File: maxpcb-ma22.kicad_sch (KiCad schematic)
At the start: 28 parts, among them P1 USB_C_Plug_USB2.0, SW1 SW_Push, U1 ATmega32U4-A, Y1 16mHz

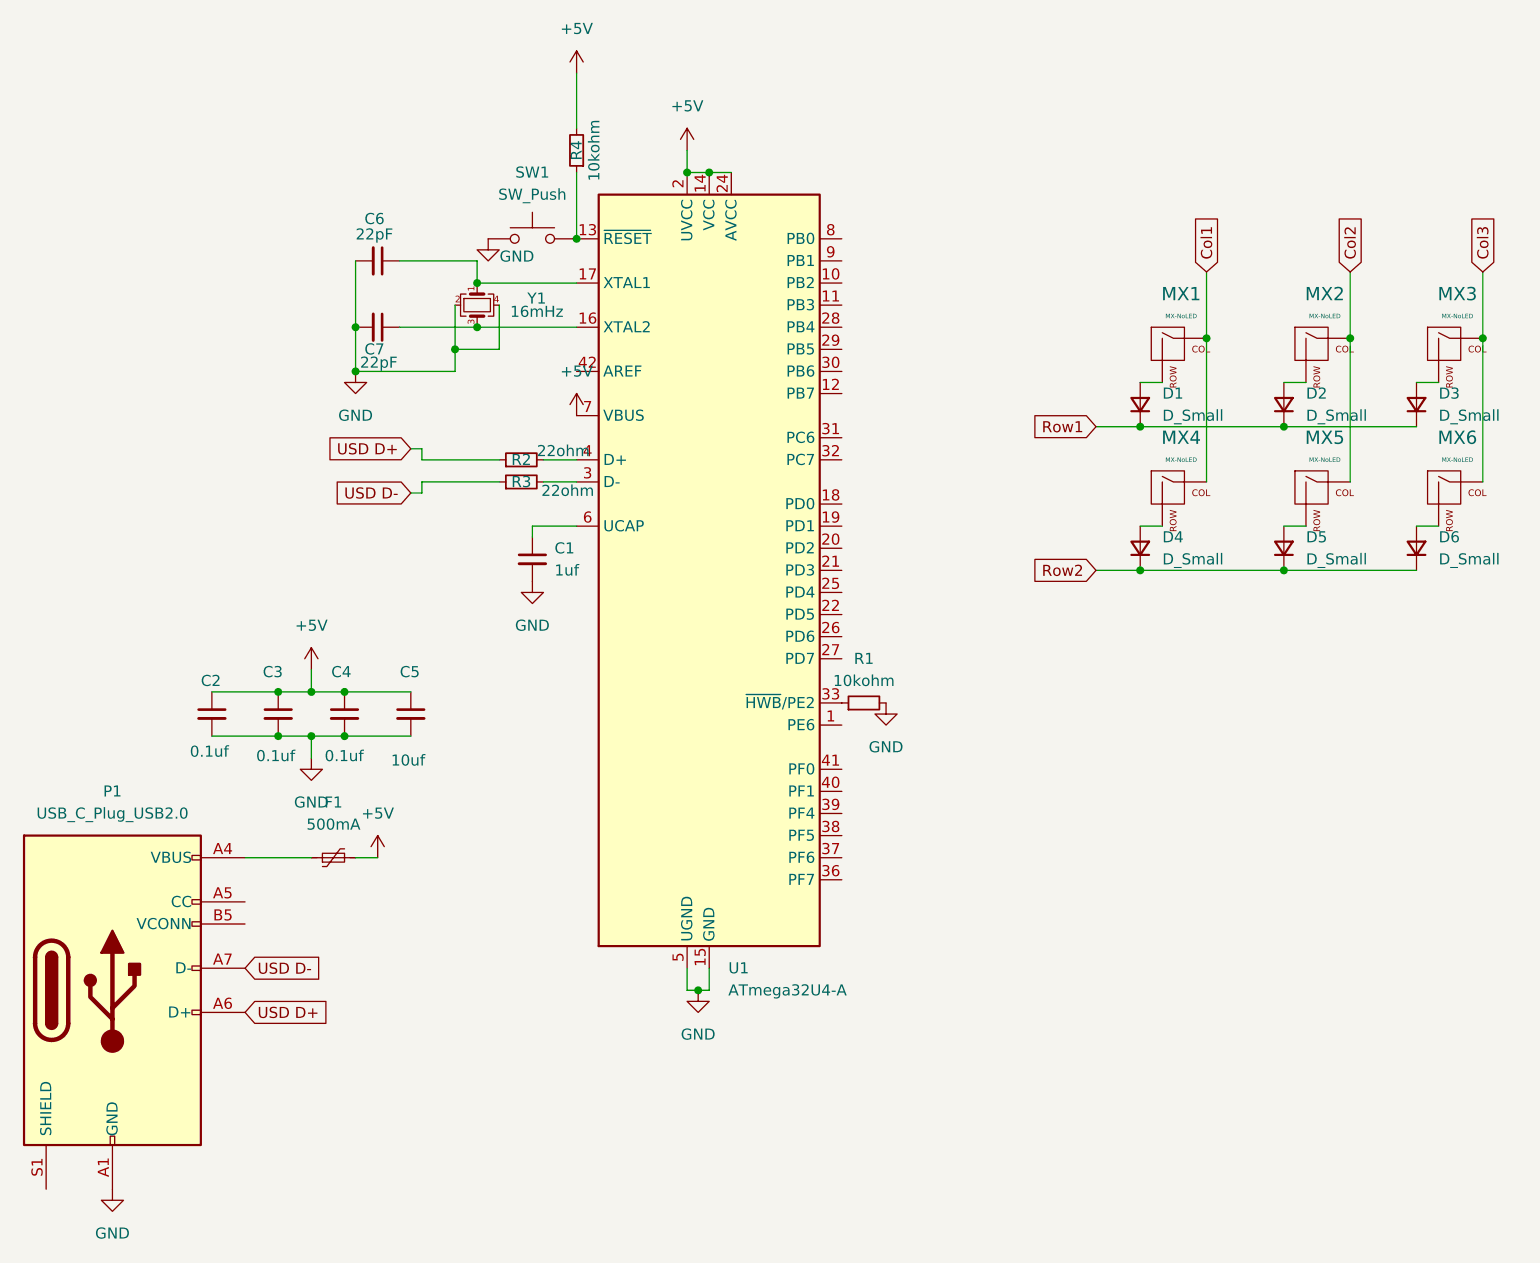
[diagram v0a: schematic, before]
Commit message: complete redo with 32u4
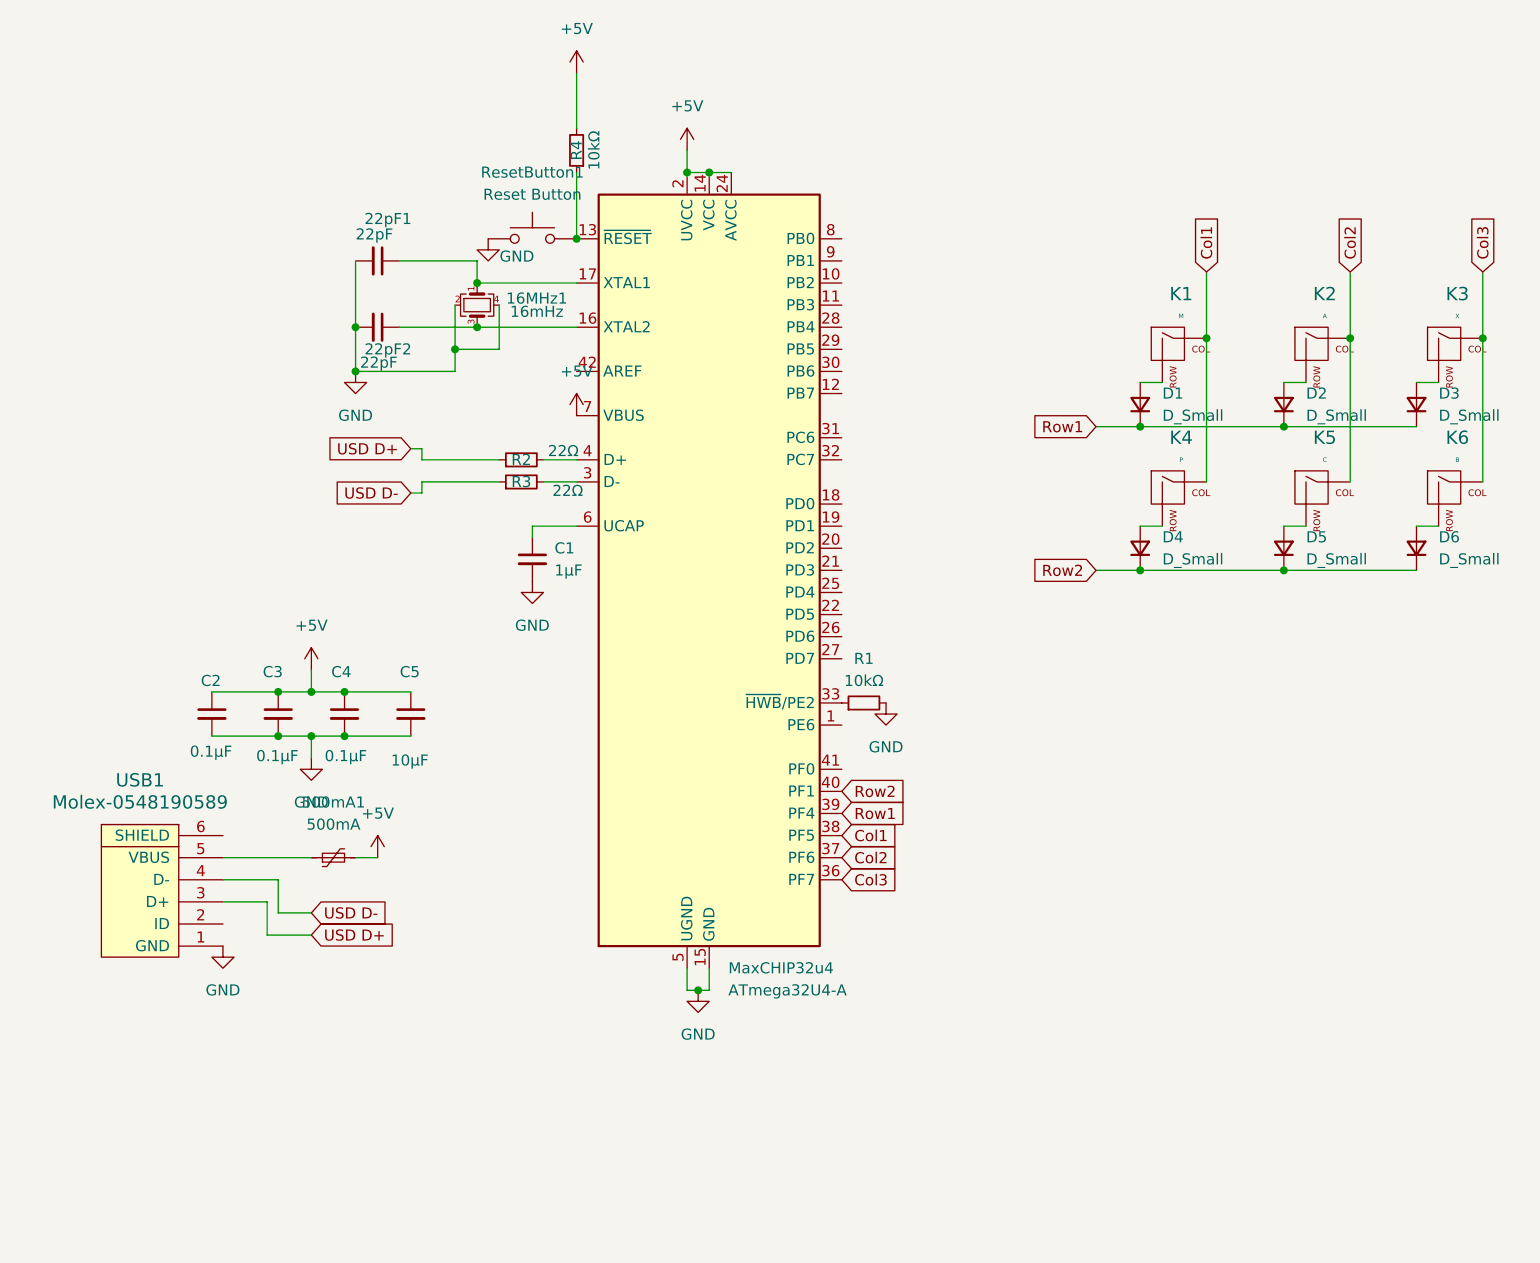
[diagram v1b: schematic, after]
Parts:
- removed P1: USB_C_Plug_USB2.0, Connector_USB:USB_C_Plug_Molex_105444, symbol Connector:USB_C_Plug_USB2.0
- added USB1: Molex-0548190589, random-keyboard-parts:Molex-0548190589, symbol random-keyboard-parts:Molex-0548190589
- 16MHz1: renamed from Y1; footprint Package_QFP:TQFP-44_10x10mm_P0.8mm -> Crystal:Crystal_SMD_3225-4Pin_3.2x2.5mm
- C1: value 1uf -> 1µF
- C2, C3, C4: value 0.1uf -> 0.1µF
- C5: value 10uf -> 10µF
- K1: renamed from MX1; value MX-NoLED -> M; footprint MX_Alps_Hybrid:MX-1U-NoLED -> MX_Only:MXOnly-1U
- K2: renamed from MX2; value MX-NoLED -> A; footprint MX_Alps_Hybrid:MX-1U-NoLED -> MX_Only:MXOnly-1U-NoLED
- K3: renamed from MX3; value MX-NoLED -> X; footprint MX_Alps_Hybrid:MX-1U-NoLED -> MX_Only:MXOnly-1U-NoLED
- K4: renamed from MX4; value MX-NoLED -> P; footprint MX_Alps_Hybrid:MX-1U-NoLED -> MX_Only:MXOnly-1U-NoLED
- K5: renamed from MX5; value MX-NoLED -> C; footprint MX_Alps_Hybrid:MX-1U-NoLED -> MX_Only:MXOnly-1U-NoLED
- K6: renamed from MX6; value MX-NoLED -> B; footprint MX_Alps_Hybrid:MX-1U-NoLED -> MX_Only:MXOnly-1U-NoLED
- R1, R4: value 10kohm -> 10kΩ
- R2, R3: value 22ohm -> 22Ω
- ResetButton1: renamed from SW1; value SW_Push -> Reset Button
- renumbered C6 to 22pF1, C7 to 22pF2, F1 to 500mA1, U1 to MaxCHIP32u4
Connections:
- net Col1: now also MaxCHIP32u4.38 (PF5)
- net Col2: now also MaxCHIP32u4.37 (PF6)
- net Col3: now also MaxCHIP32u4.36 (PF7)
- net GND: now also USB1.1 (GND)
- net Row1: now also MaxCHIP32u4.39 (PF4)
- net Row2: now also MaxCHIP32u4.40 (PF1)
- net USD D+: now also USB1.3 (D+)
- net USD D-: now also USB1.4 (D-)
- net at 500mA1.1: now also USB1.5 (VBUS)
